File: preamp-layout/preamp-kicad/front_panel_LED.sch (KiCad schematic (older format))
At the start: 40 parts

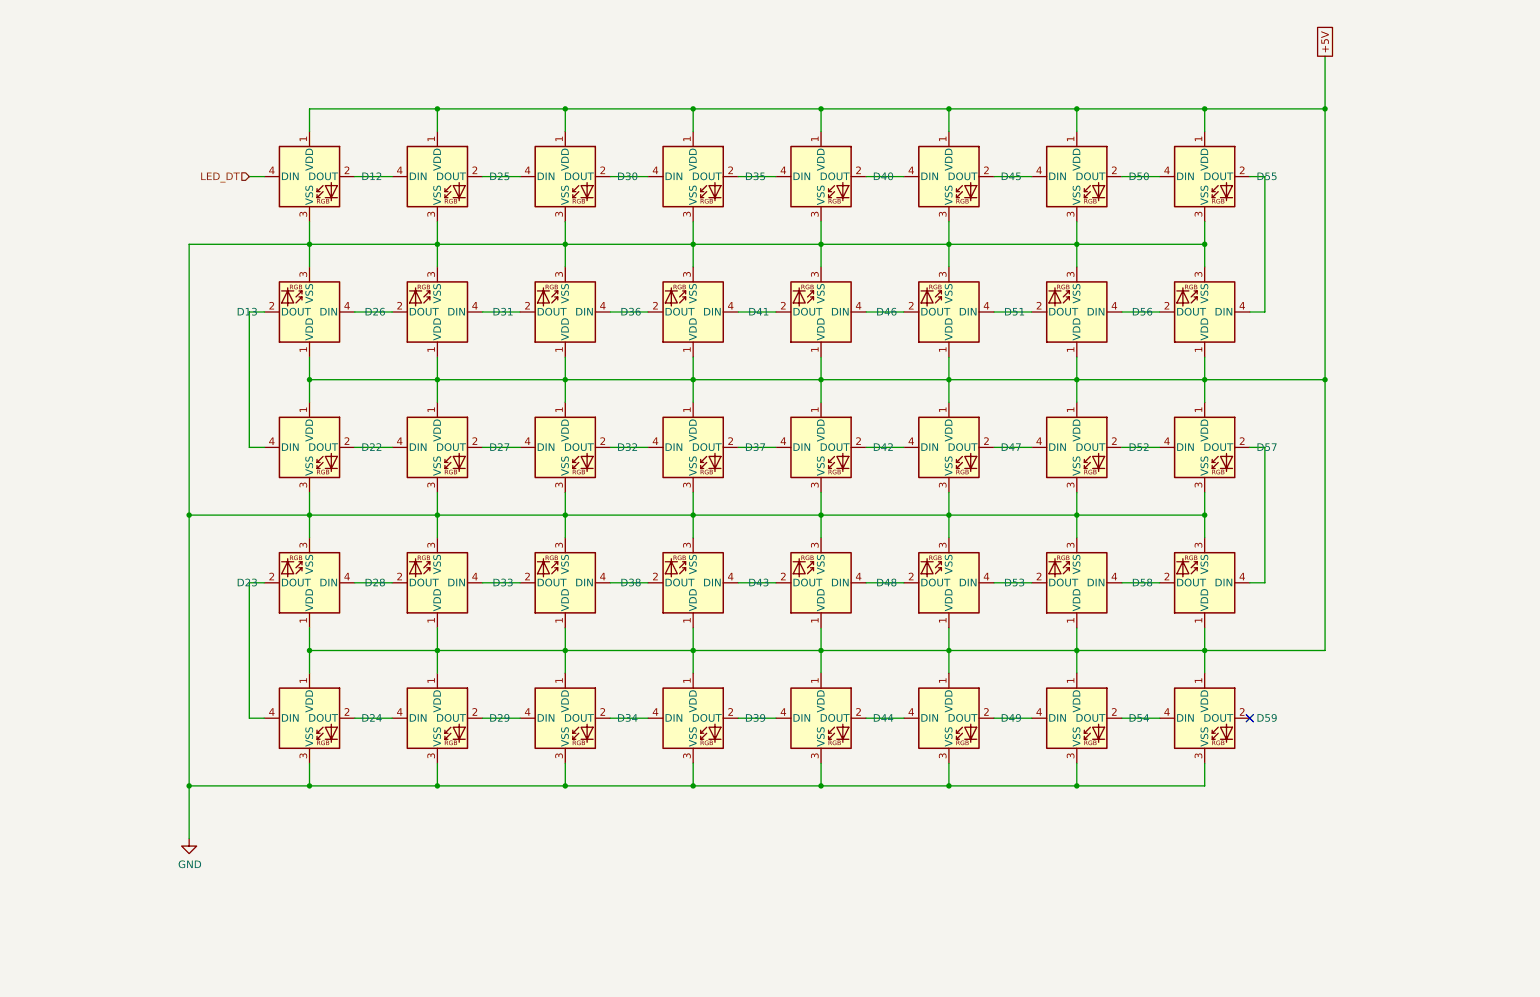
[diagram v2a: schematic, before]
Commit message: BOM Update
parts added to BOM, connector cleanup. Stopping point before renumbering refdes in a more intelligent way.
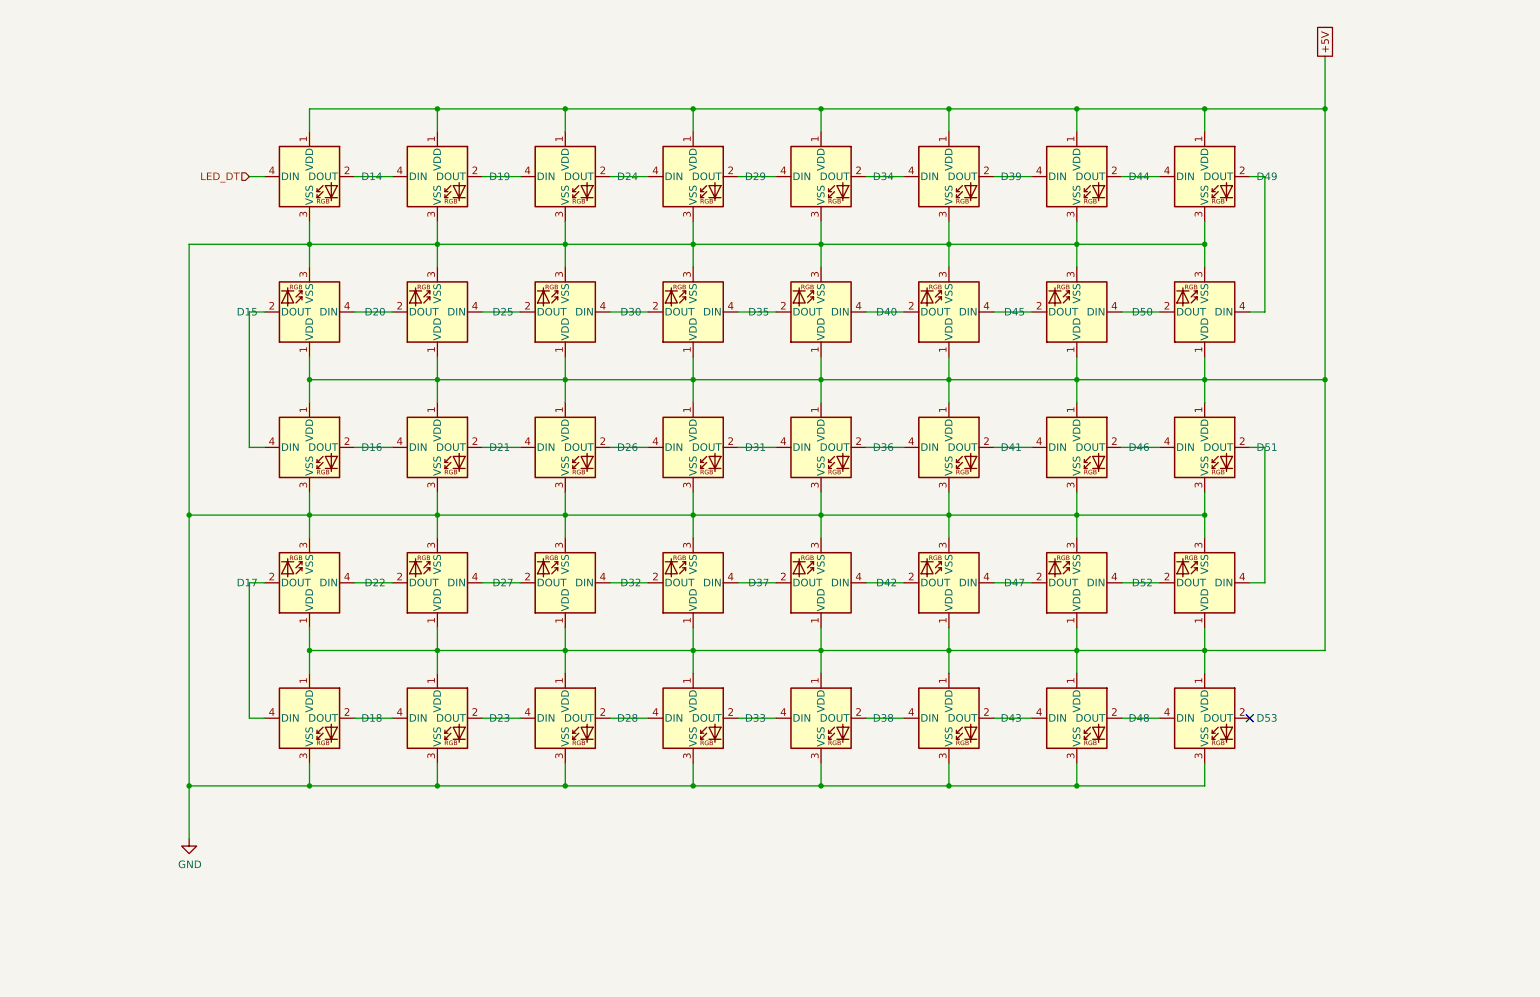
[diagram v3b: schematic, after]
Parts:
- renumbered D12 to D14, D13 to D15, D22 to D16, D23 to D17, D24 to D18, D25 to D19, D26 to D20, D27 to D21, D28 to D22, D29 to D23, D30 to D24, D31 to D25, D32 to D26, D33 to D27, D34 to D28, D35 to D29, D36 to D30, D37 to D31, D38 to D32, D39 to D33, D40 to D34, D41 to D35, D42 to D36, D43 to D37, D44 to D38, D45 to D39, D46 to D40, D47 to D41, D48 to D42, D49 to D43, D50 to D44, D51 to D45, D52 to D46, D53 to D47, D54 to D48, D55 to D49, D56 to D50, D57 to D51, D58 to D52, D59 to D53

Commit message: Minor Updates
Moved headphone jack to amp pcb. I2C pin updates. Added caps to LED light strip. Added 0.1uF caps to all ICs.
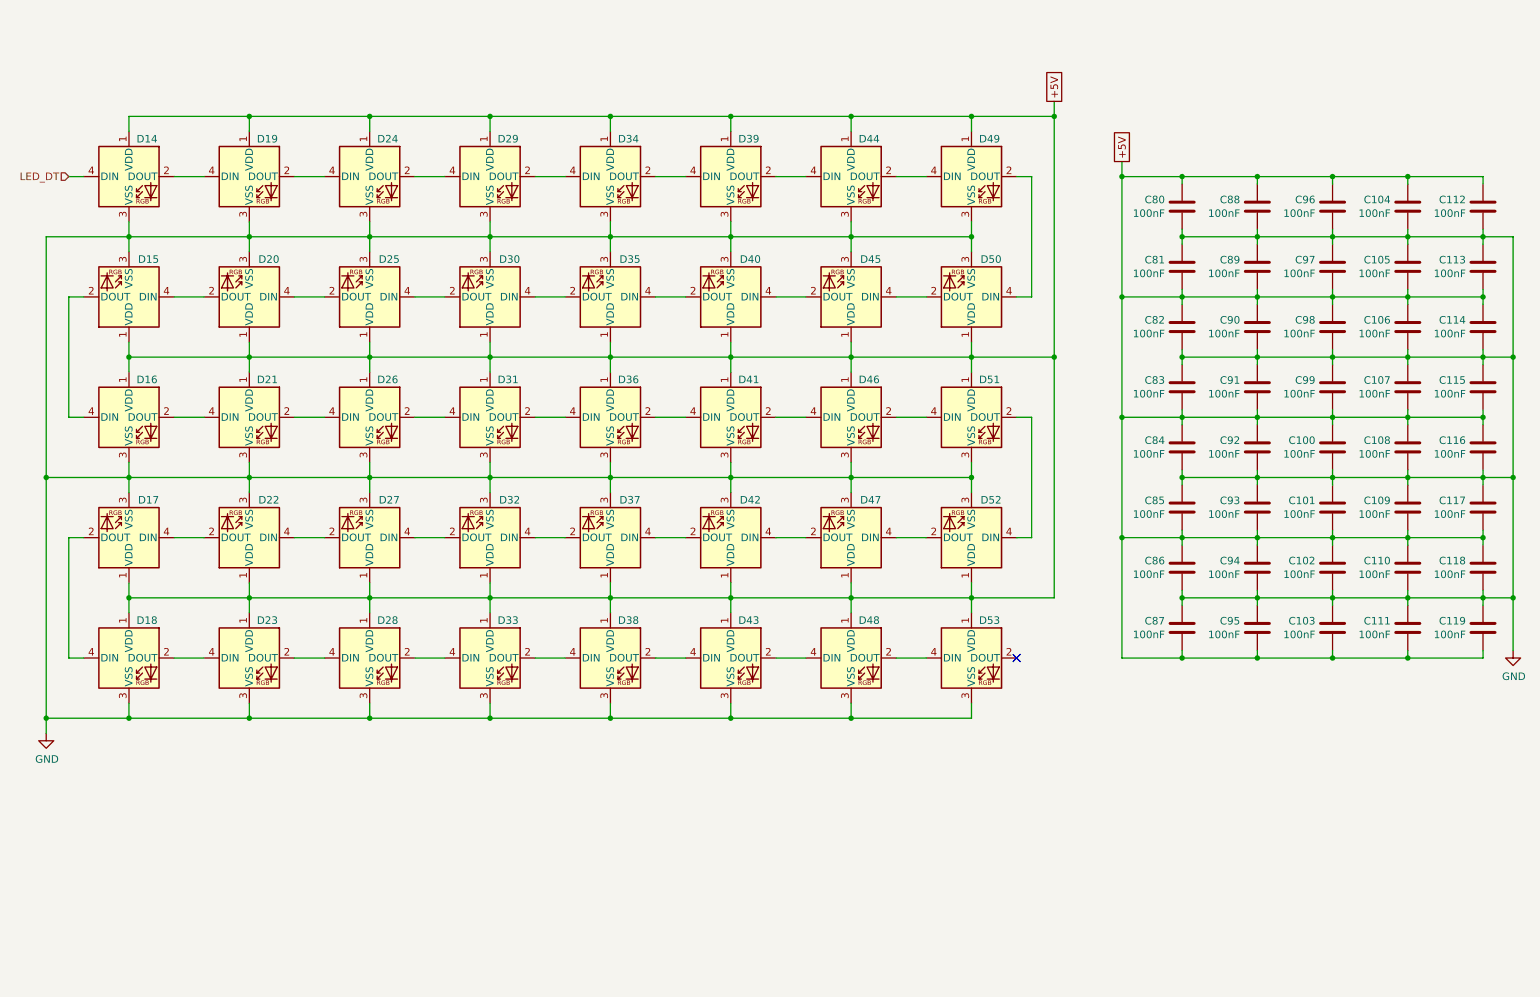
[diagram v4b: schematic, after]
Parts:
- added C100, C101, C102, C103, C104, C105, C106, C107, C108, C109, C110, C111, C112, C113, C114, C115, C116, C117, C118, C119, C80, C81, C82, C83, C84, C85, C86, C87, C88, C89, C90, C91, C92, C93, C94, C95, C96, C97, C98, C99: 100nF, Capacitor_SMD:C_0805_2012Metric_Pad1.15x1.40mm_HandSolder, symbol Device:C
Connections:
- net +5V: now also C100.1, C101.2, C102.1, C103.2, C104.1, C105.2, C106.1, C107.2, C108.1, C109.2, C110.1, C111.2, C112.1, C113.2, C114.1, C115.2, C116.1, C117.2, C118.1, C119.2, C80.1, C81.2, C82.1, C83.2, C84.1, C85.2, C86.1, C87.2, C88.1, C89.2, C90.1, C91.2, C92.1, C93.2, C94.1, C95.2, C96.1, C97.2, C98.1, C99.2
- net GND: now also C100.2, C101.1, C102.2, C103.1, C104.2, C105.1, C106.2, C107.1, C108.2, C109.1, C110.2, C111.1, C112.2, C113.1, C114.2, C115.1, C116.2, C117.1, C118.2, C119.1, C80.2, C81.1, C82.2, C83.1, C84.2, C85.1, C86.2, C87.1, C88.2, C89.1, C90.2, C91.1, C92.2, C93.1, C94.2, C95.1, C96.2, C97.1, C98.2, C99.1
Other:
- moved on the sheet: D14, D15, D16, D17, D18, D19, D20, D21, D22, D23, D24, D25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

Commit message: RefDes Update
Re-ran refdes assignment, updated BOM accordingly.
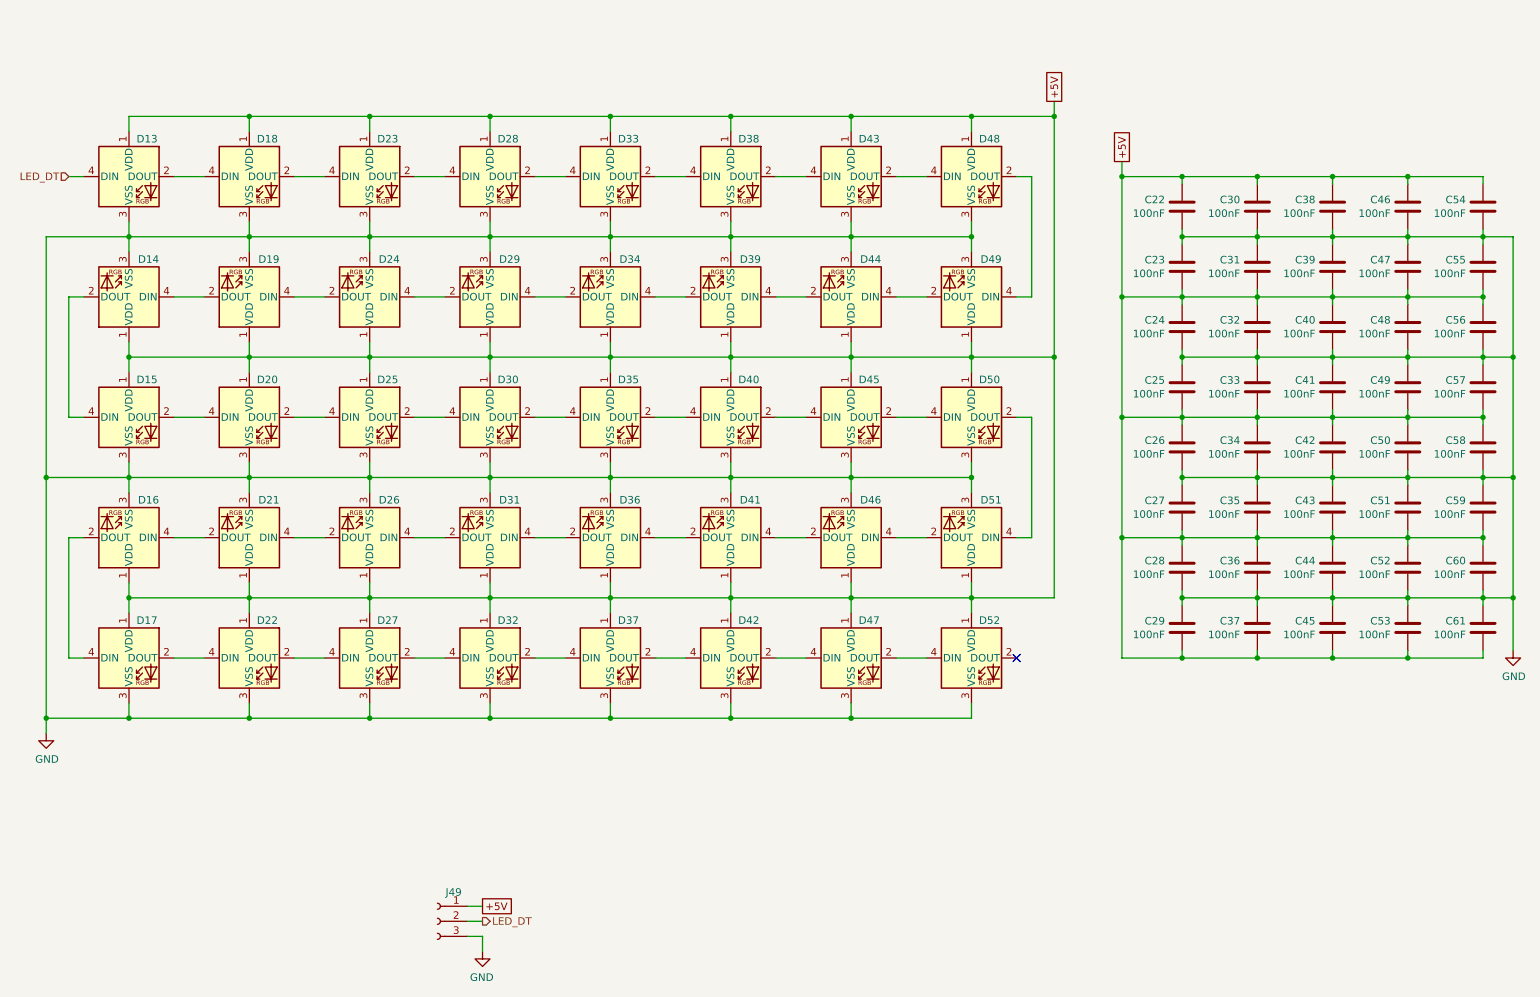
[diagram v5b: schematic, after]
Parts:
- added J49: Conn_01x03_Female, symbol Connector:Conn_01x03_Female
- renumbered C80 to C22, C81 to C23, C82 to C24, C83 to C25, C84 to C26, C85 to C27, C86 to C28, C87 to C29, C88 to C30, C89 to C31, C90 to C32, C91 to C33, C92 to C34, C93 to C35, C94 to C36, C95 to C37, C96 to C38, C97 to C39, C98 to C40, C99 to C41, C100 to C42, C101 to C43, C102 to C44, C103 to C45, C104 to C46, C105 to C47, C106 to C48, C107 to C49, C108 to C50, C109 to C51, C110 to C52, C111 to C53, C112 to C54, C113 to C55, C114 to C56, C115 to C57, C116 to C58, C117 to C59, C118 to C60, C119 to C61, D14 to D13, D15 to D14, D16 to D15, D17 to D16, D18 to D17, D19 to D18, D20 to D19, D21 to D20, D22 to D21, D23 to D22, D24 to D23, D25 to D24, D26 to D25, D27 to D26, D28 to D27, D29 to D28, D30 to D29, D31 to D30, D32 to D31, D33 to D32, D34 to D33, D35 to D34, D36 to D35, D37 to D36, D38 to D37, D39 to D38, D40 to D39, D41 to D40, D42 to D41, D43 to D42, D44 to D43, D45 to D44, D46 to D45, D47 to D46, D48 to D47, D49 to D48, D50 to D49, D51 to D50, D52 to D51, D53 to D52
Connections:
- net +5V: now also J49.1 (Pin_1)
- net GND: now also J49.3 (Pin_3)
- net LED_DT: now also J49.2 (Pin_2)

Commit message: Prelim PCB layout
Work done to lay out PCBs. Saving in anticipation of creating branch with a different input switching topology.
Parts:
- J49: footprint (none) -> Connector_PinHeader_2.54mm:PinHeader_1x03_P2.54mm_Vertical
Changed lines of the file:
@@
 F 0 "J49" H 3492 7093 50  0000 C CNN
 F 1 "Conn_01x03_Female" H 3492 7094 50  0001 C CNN
-F 2 "" H 3600 6900 50  0001 C CNN
+F 2 "Connector_PinHeader_2.54mm:PinHeader_1x03_P2.54mm_Vertical" H 3600 6900 50  0001 C CNN
 F 3 "~" H 3600 6900 50  0001 C CNN
 	1    3600 6900

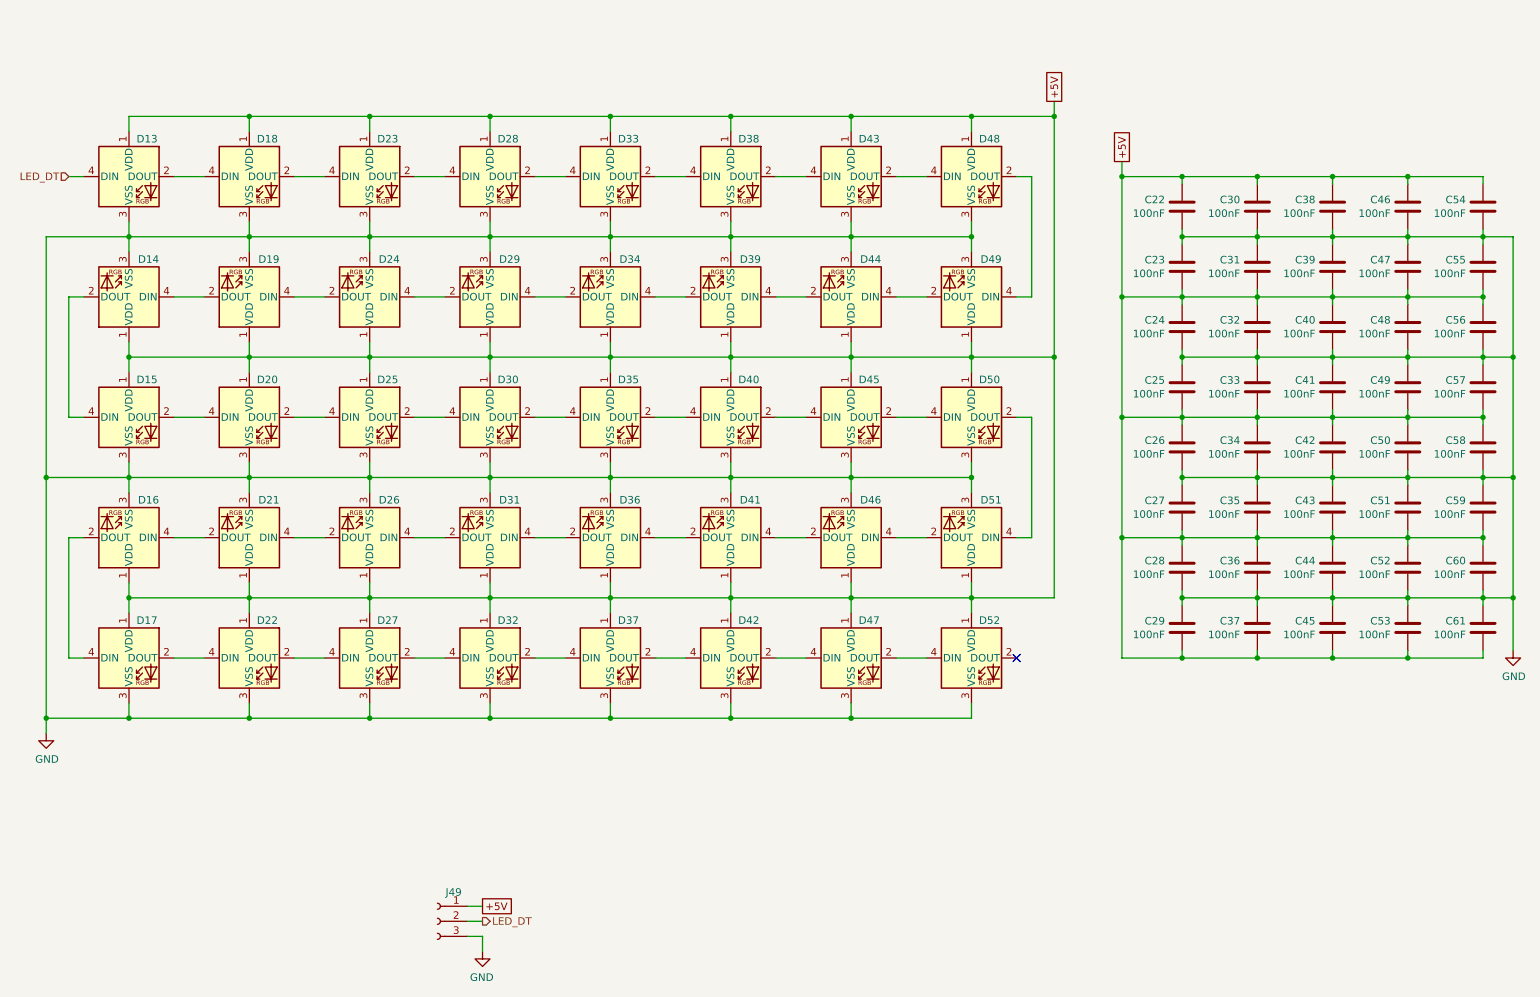
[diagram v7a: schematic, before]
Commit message: PCB layout update, front panel and LED restructure
Restructure of capacitive buttons. Restructure of MCU schematic. Moved LEDs to front panel sheet. Front panel and MCU initial PCB layout. 8 bit DAC update (grounded address pins). DAC connection renaming. Added mounting holes for boards.
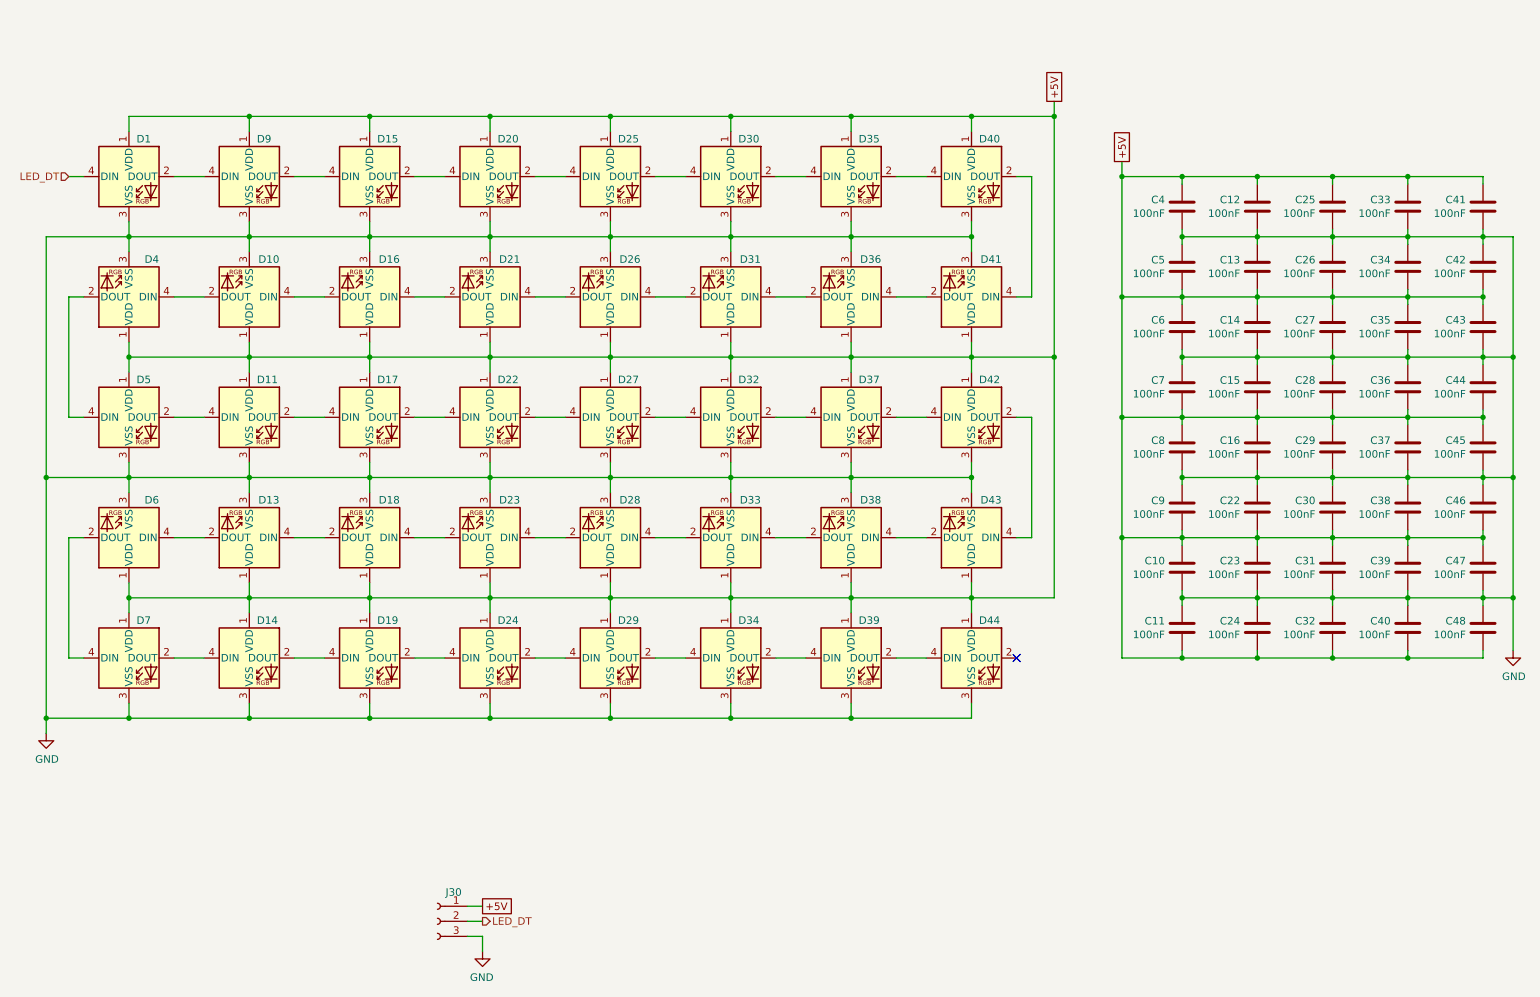
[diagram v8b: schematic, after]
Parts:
- J49: footprint Connector_PinHeader_2.54mm:PinHeader_1x03_P2.54mm_Vertical -> Connector_JST:JST_EH_S3B-EH_1x03_P2.50mm_Horizontal
